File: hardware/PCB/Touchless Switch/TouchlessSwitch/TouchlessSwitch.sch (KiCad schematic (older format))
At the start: 12 parts, among them K1 Screw_Terminal_01x02, K2 Screw_Terminal_01x02, K3 Pinheader, T1 BC337

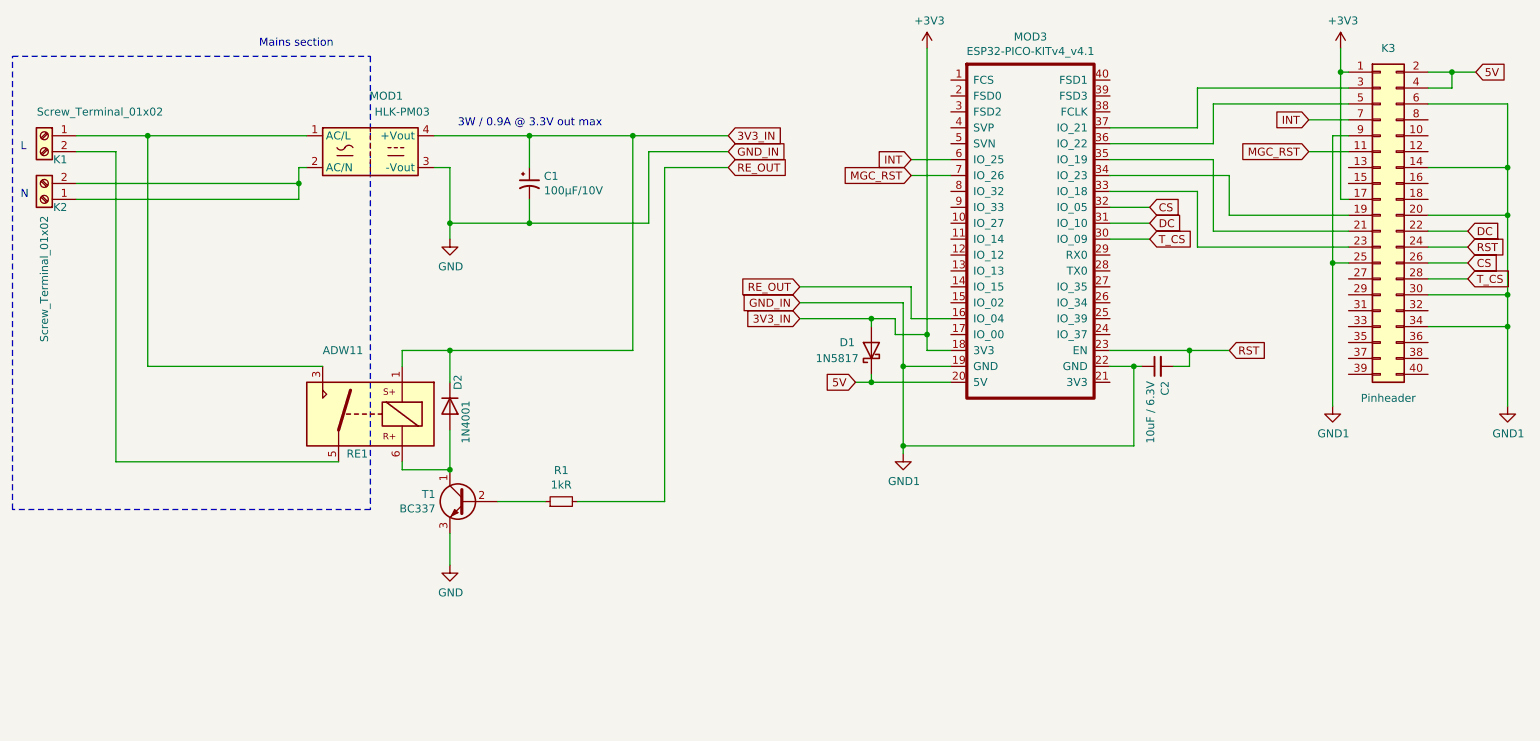
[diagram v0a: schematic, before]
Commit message: PCB Files Update for latching relay
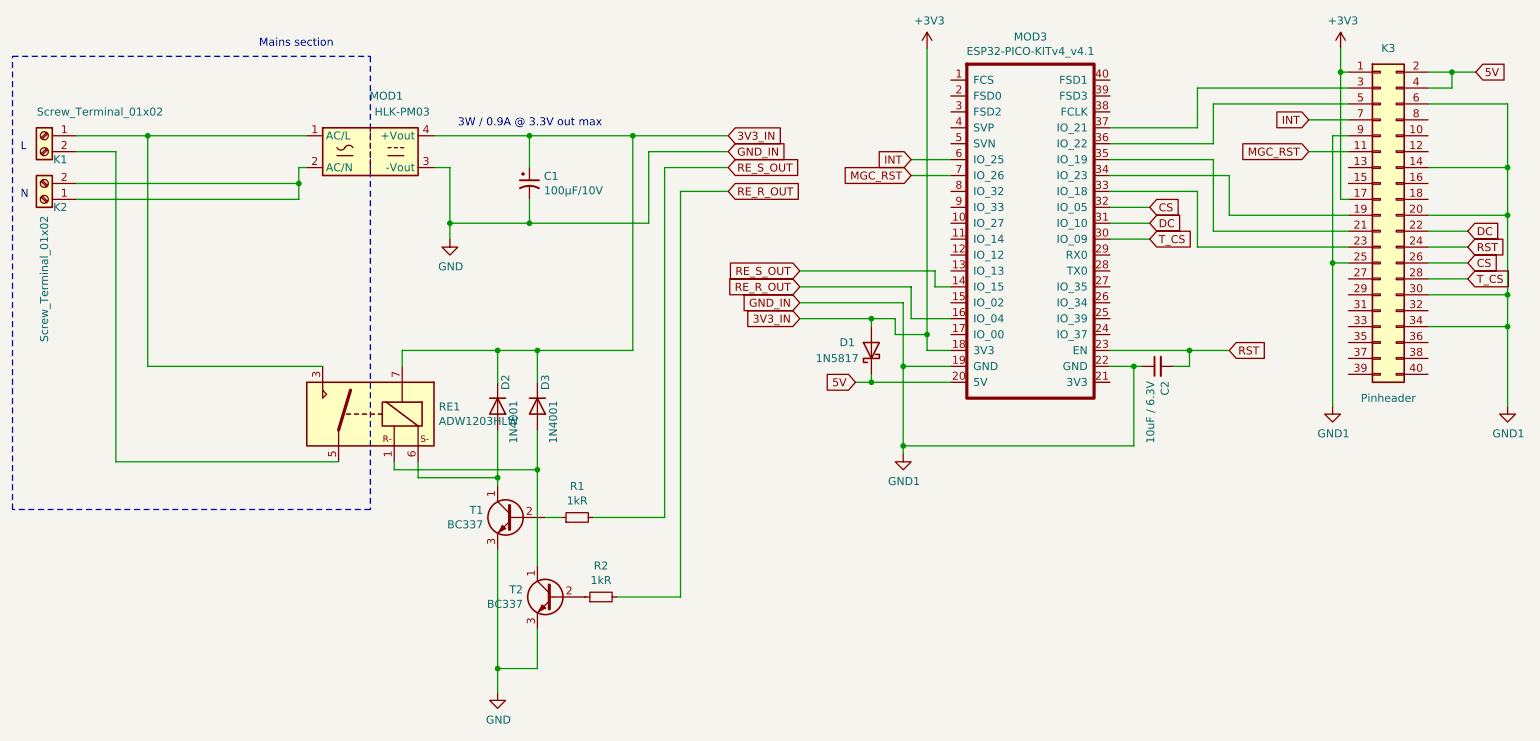
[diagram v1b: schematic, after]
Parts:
- removed RE1: ADW11, Relay_THT:Relay_1P1T_NO_10x24x18.8mm_Panasonic_ADW11xxxxW_THT, symbol Relay:ADW11
- added D3: 1N4001, Diode_THT:D_DO-41_SOD81_P7.62mm_Horizontal, symbol Device:D
- added R2: 1kR, Resistor_THT:R_Axial_DIN0207_L6.3mm_D2.5mm_P10.16mm_Horizontal, symbol Device:R_Small
- added RE1: ADW1203HLW, ADW1203HLW:Relay_1P1T_NO_10x24x18.8mm_Panasonic_ADW11xxxxW_THT, symbol ADW1203HLW:ADW1203HLW
- added T2: BC337, Package_TO_SOT_THT:TO-92_Inline, symbol Transistor_BJT:BC337
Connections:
- net +3V3: now also D3.1 (K), RE1.7
- net GND: now also T2.3 (E)
- net at K1.1 (Pin_1), MOD1.1 (AC/L): now also RE1.3
- net RE_S_OUT: now reaches MOD3.14 (IO_15)
- net RE_S_OUT: now also R1.2
- net at K1.2 (Pin_2): now also RE1.5
- net at D2.2 (A), T1.1 (C): now also RE1.6
- net RE_OUT renamed RE_R_OUT
- net RE_R_OUT: now also R2.2; no longer R1.2
- new net: D3.2 (A), RE1.1, T2.1 (C)
- new net: R2.1, T2.2 (B)
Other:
- moved on the sheet: D2, R1, T1
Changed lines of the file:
@@
 Wire Wire Line
 	6650 3750 6650 3800
-$Comp
-L Relay:ADW11 RE1
-U 1 1 605B7F3A
-P 3300 3550
-F 0 "RE1" H 3450 3300 50  0000 R CNN
-F 1 "ADW11" H 3600 3950 50  0000 R CNN
-F 2 "Relay_THT:Relay_1P1T_NO_10x24x18.8mm_Panasonic_ADW11xxxxW_THT" H 4625 3500 50  0001 C CNN
-F 3 "https://www.panasonic-electric-works.com/pew/es/downloads/ds_dw_hl_en.pdf" H 3300 3550 50  0001 C CNN
-	1    3300 3550
-	-1   0    0    -1
-$EndComp
 Text Notes 3850 1750 0    50   ~ 0
 3W / 0.9A @ 3.3V out max
-Wire Wire Line
-	3500 3850 3500 3900
-Wire Wire Line
-	3500 3150 3500 3250
 $Comp
 L Connector_Generic:Conn_02x20_Odd_Even K3
@@
 L Device:D D2
 U 1 1 606140AD
-P 3800 3500
-F 0 "D2" H 3650 3550 50  0000 C CNN
-F 1 "1N4001" H 3900 3600 50  0000 C CNN
-F 2 "Diode_THT:D_DO-41_SOD81_P7.62mm_Horizontal" H 3800 3500 50  0001 C CNN
-F 3 "~" H 3800 3500 50  0001 C CNN
-	1    3800 3500
+P 4100 3500
+F 0 "D2" H 3950 3550 50  0000 C CNN
+F 1 "1N4001" H 4200 3600 50  0000 C CNN
+F 2 "Diode_THT:D_DO-41_SOD81_P7.62mm_Horizontal" H 4100 3500 50  0001 C CNN
+F 3 "~" H 4100 3500 50  0001 C CNN
+	1    4100 3500
 	0    1    1    0
 $EndComp
@@
 	1700 3850 3100 3850
 Wire Wire Line
-	3500 3150 3800 3150
-Wire Wire Line
-	3800 3150 3800 3350
-Wire Wire Line
-	3800 3650 3800 3900
-Wire Wire Line
-	3800 3900 3500 3900
+	4100 3150 4100 3350
+Wire Wire Line
+	4100 3650 4100 3950
 $Comp
 L power:GND #PWR0106
 U 1 1 60654EB1
-P 3800 4500
-F 0 "#PWR0106" H 3800 4250 50  0001 C CNN
-F 1 "GND" H 3805 4327 50  0000 C CNN
-F 2 "" H 3800 4500 50  0001 C CNN
-F 3 "" H 3800 4500 50  0001 C CNN
-	1    3800 4500
+P 4100 5300
+F 0 "#PWR0106" H 4100 5050 50  0001 C CNN
+F 1 "GND" H 4105 5127 50  0000 C CNN
+F 2 "" H 4100 5300 50  0001 C CNN
+F 3 "" H 4100 5300 50  0001 C CNN
+	1    4100 5300
 	1    0    0    -1
 $EndComp
@@
 L Transistor_BJT:BC337 T1
 U 1 1 606986AF
-P 3900 4100
-F 0 "T1" H 4091 4146 50  0000 L CNN
-F 1 "BC337" H 4091 4055 50  0000 L CNN
-F 2 "Package_TO_SOT_THT:TO-92_Inline" H 4100 4025 50  0001 L CIN
-F 3 "https://diotec.com/tl_files/diotec/files/pdf/datasheets/bc337.pdf" H 3900 4100 50  0001 L CNN
-	1    3900 4100
+P 4200 4200
+F 0 "T1" H 4391 4246 50  0000 L CNN
+F 1 "BC337" H 4391 4155 50  0000 L CNN
+F 2 "Package_TO_SOT_THT:TO-92_Inline" H 4400 4125 50  0001 L CIN
+F 3 "https://diotec.com/tl_files/diotec/files/pdf/datasheets/bc337.pdf" H 4200 4200 50  0001 L CNN
+	1    4200 4200
 	-1   0    0    -1
 $EndComp
-Connection ~ 3800 3900
 $Comp
 L Device:R_Small R1
 U 1 1 606A6FD4
-P 4500 4100
-F 0 "R1" V 4696 4100 50  0000 C CNN
-F 1 "1kR" V 4605 4100 50  0000 C CNN
-F 2 "Resistor_THT:R_Axial_DIN0207_L6.3mm_D2.5mm_P10.16mm_Horizontal" H 4500 4100 50  0001 C CNN
-F 3 "~" H 4500 4100 50  0001 C CNN
-	1    4500 4100
+P 4600 4200
+F 0 "R1" V 4796 4200 50  0000 C CNN
+F 1 "1kR" V 4705 4200 50  0000 C CNN
+F 2 "Resistor_THT:R_Axial_DIN0207_L6.3mm_D2.5mm_P10.16mm_Horizontal" H 4600 4200 50  0001 C CNN
+F 3 "~" H 4600 4200 50  0001 C CNN
+	1    4600 4200
 	0    -1   -1   0
 $EndComp
 Wire Wire Line
-	3800 4300 3800 4500
-Wire Wire Line
-	4100 4100 4400 4100
-Wire Wire Line
 	4950 1800 4950 3150
 Wire Wire Line
 	5050 2350 5050 1900
 Wire Wire Line
-	5150 2000 5150 4100
-Wire Wire Line
-	4600 4100 5150 4100
+	5150 2000 5150 4200
 Wire Wire Line
 	8450 3150 8700 3150
@@
 Wire Wire Line
 	6450 3350 6950 3350
-Text GLabel 6000 2750 0    50   Input ~ 0
-RE_OUT
 Text GLabel 5550 1800 2    50   Input ~ 0
 3V3_IN
@@
 GND_IN
 Text GLabel 5550 2000 2    50   Input ~ 0
-RE_OUT
+RE_S_OUT
 Text GLabel 6000 2850 0    50   Input ~ 0
 GND_IN
@@
 	4300 1800 4950 1800
 Wire Wire Line
-	3800 3150 4950 3150
-Connection ~ 3800 3150
+	4100 3150 4350 3150
+$Comp
+L ADW1203HLW:ADW1203HLW RE1
+U 1 1 615994E7
+P 3300 3550
+F 0 "RE1" H 2870 3596 50  0000 R CNN
+F 1 "ADW1203HLW" H 2870 3505 50  0000 R CNN
+F 2 "ADW1203HLW:Relay_1P1T_NO_10x24x18.8mm_Panasonic_ADW11xxxxW_THT" H 2850 3800 50  0001 C CNN
+F 3 "" H 2850 3800 50  0001 C CNN
+	1    3300 3550
+	-1   0    0    -1
+$EndComp
+Wire Wire Line
+	4100 3150 3500 3150
+Wire Wire Line
+	3500 3150 3500 3250
+Connection ~ 4100 3150
+Wire Wire Line
+	3600 3850 3600 3950
+Wire Wire Line
+	3600 3950 4100 3950
+Connection ~ 4100 3950
+Wire Wire Line
+	4100 3950 4100 4000
+$Comp
+L Transistor_BJT:BC337 T2
+U 1 1 615B5229
+P 4450 4700
+F 0 "T2" H 4641 4746 50  0000 L CNN
+F 1 "BC337" H 4641 4655 50  0000 L CNN
+F 2 "Package_TO_SOT_THT:TO-92_Inline" H 4650 4625 50  0001 L CIN
+F 3 "https://diotec.com/tl_files/diotec/files/pdf/datasheets/bc337.pdf" H 4450 4700 50  0001 L CNN
+	1    4450 4700
+	-1   0    0    -1
+$EndComp
+$Comp
+L Device:R_Small R2
+U 1 1 615B522F
+P 4750 4700
+F 0 "R2" V 4946 4700 50  0000 C CNN
+F 1 "1kR" V 4855 4700 50  0000 C CNN
+F 2 "Resistor_THT:R_Axial_DIN0207_L6.3mm_D2.5mm_P10.16mm_Horizontal" H 4750 4700 50  0001 C CNN
+F 3 "~" H 4750 4700 50  0001 C CNN
+	1    4750 4700
+	0    -1   -1   0
+$EndComp
+Wire Wire Line
+	3450 3850 3450 3900
+Wire Wire Line
+	4350 4900 4350 5150
+$Comp
+L Device:D D3
+U 1 1 615EB1B2
+P 4350 3500
+F 0 "D3" H 4200 3550 50  0000 C CNN
+F 1 "1N4001" H 4450 3600 50  0000 C CNN
+F 2 "Diode_THT:D_DO-41_SOD81_P7.62mm_Horizontal" H 4350 3500 50  0001 C CNN
+F 3 "~" H 4350 3500 50  0001 C CNN
+	1    4350 3500
+	0    1    1    0
+$EndComp
+Wire Wire Line
+	3450 3900 4350 3900
+Wire Wire Line
+	4350 3900 4350 3650
+Wire Wire Line
+	4350 3350 4350 3150
+Connection ~ 4350 3150
+Wire Wire Line
+	4350 3150 4950 3150
+Wire Wire Line
+	4400 4200 4500 4200
+Wire Wire Line
+	4350 3900 4350 4500
+Connection ~ 4350 3900
+Wire Wire Line
+	4350 5150 4100 5150
+Wire Wire Line
+	4100 4400 4100 5150
+Connection ~ 4100 5150
+Wire Wire Line
+	4100 5150 4100 5300
+Wire Wire Line
+	4700 4200 5150 4200
+Wire Wire Line
+	4850 4700 5250 4700
+Wire Wire Line
+	5250 4700 5250 2150
+Wire Wire Line
+	5250 2150 5550 2150
+Text GLabel 5550 2150 2    50   Input ~ 0
+RE_R_OUT
+Text GLabel 6000 2750 0    50   Input ~ 0
+RE_R_OUT
+Text GLabel 6000 2650 0    50   Input ~ 0
+RE_S_OUT
+Wire Wire Line
+	6950 2750 6850 2750
+Wire Wire Line
+	6850 2750 6850 2650
+Wire Wire Line
+	6850 2650 6000 2650
 $EndSCHEMATC
